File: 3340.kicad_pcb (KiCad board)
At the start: 2 copper layers, 110.5 x 106.7 mm, 181 parts, among them J1 Conn_01x17, J10 FM1, J11 Conn_01x17, J12 V/OCT2, J13 PULSE2, J14 SAW2, J15 TRI2, J16 SINE2, J17 SYNC2, J18 Conn_01x17, J19 PWM2, J2 Conn_01x17, J20 FM2, J3 V/OCT1, J4 PULSE1, J5 SAW1, J6 TRI1, J7 SINE1, J8 SYNC1, J9 PWM1, Q1 2N3904, Q2 2N3906, Q3 2N3904, Q4 2N3906, Q5 2N3904, Q6 2N3904, SW2 DPDT_OOO, U1 TL072, U2 TL074, U3 CEM3340, U4 TL072, U5 CEM3340, U6 TL074

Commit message: Fix electrolytic footprints
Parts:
- removed D7, D8: 1N5818, Diode_THT:D_DO-41_SOD81_P10.16mm_Horizontal
- removed PWR2: PWR, Connector_IDC:IDC-Header_2x05_P2.54mm_Vertical
- moved PWR1 230.2 mm to (19.6, 132.1)
- moved D1 230.2 mm to (27.7, 150.1)
- moved D2 230.2 mm to (27.7, 153.7)
- moved J1 76.4 mm to (121.3, 47.0)
- moved COARSE2 0.65 mm to (41.9, 26.0)
- moved FINE2 0.65 mm to (54.6, 26.0)
- moved J13 0.65 mm to (45.1, 91.4)
- moved J14 0.65 mm to (57.8, 91.4)
- moved J15 0.65 mm to (45.1, 105.3)
- moved J16 0.65 mm to (57.8, 105.3)
- moved J19 0.65 mm to (42.5, 73.6)
- moved J4 0.65 mm to (18.4, 91.4)
- moved J5 0.65 mm to (31.1, 91.4)
- moved J6 0.65 mm to (18.4, 105.3)
- moved J7 0.65 mm to (31.1, 105.3)
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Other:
- board size 110.5 x 106.7 mm -> 110.5 x 106 mm

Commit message: Start backboard 1
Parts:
- C14, C15: footprint Capacitor_THT:C_Disc_D4.3mm_W1.9mm_P5.00mm -> Capacitor_THT:CP_Radial_D5.0mm_P2.00mm
- moved C5 302.4 mm to (86.0, 17.0)
- moved C13 301.6 mm to (64.0, 59.0)
- moved TRK1 287.2 mm to (95.0, 94.0)
- moved C14 287.1 mm to (75.6, 112.3), turned to -90 degrees
- moved R26 278.1 mm to (66.0, 48.0)
- moved U1 277.9 mm to (103.5, 62.9), turned to 180 degrees
- moved C12 276.2 mm to (70.0, 80.0)
- moved R27 273.8 mm to (79.0, 52.0)
- moved C15 265.2 mm to (75.6, 96.8), turned to -90 degrees
- moved R1 264.8 mm to (93.4, 59.7), turned to 180 degrees
- moved R28 261.4 mm to (64.0, 54.0)
- moved C19 260.8 mm to (70.0, 73.0)
- moved D4 258.6 mm to (74.9, 93.3), turned to 180 degrees
- moved R6 256.1 mm to (85.0, 112.0)
- moved C4 254.0 mm to (69.0, 66.0)
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
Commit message: Use autoplace from here
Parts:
- moved C18 270.4 mm to (101.6, 72.7), turned to 180 degrees
- moved R40 269.2 mm to (74.9, 38.7)
- moved C6 168.0 mm to (126.4, 194.3)
- moved C7 161.7 mm to (126.4, 181.6)
- moved D1 158.5 mm to (132.1, 185.4)
- moved C16 144.3 mm to (126.4, 186.1)
- moved C13 139.4 mm to (121.3, 186.1)
- moved R14 135.6 mm to (130.2, 156.8)
- moved R19 125.6 mm to (116.8, 156.8)
- moved R34 124.1 mm to (76.8, 143.9)
- moved C12 121.8 mm to (121.3, 190.5)
- moved R28 118.6 mm to (130.2, 152.4)
- moved R17 118.4 mm to (130.8, 144.8)
- moved C8 118.3 mm to (126.4, 190.5)
- moved R27 107.5 mm to (117.5, 152.4)
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
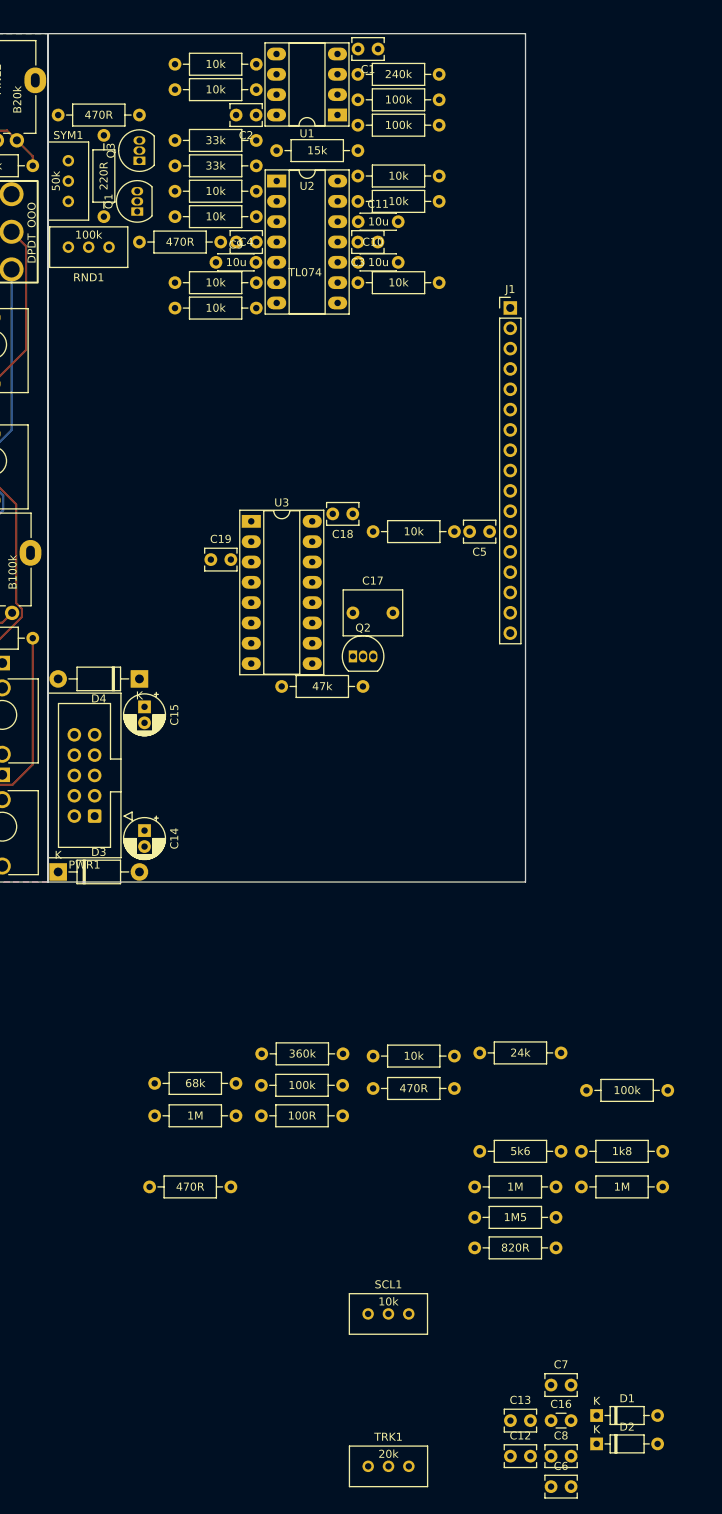
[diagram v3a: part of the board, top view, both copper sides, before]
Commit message: Fix PWM2 connection
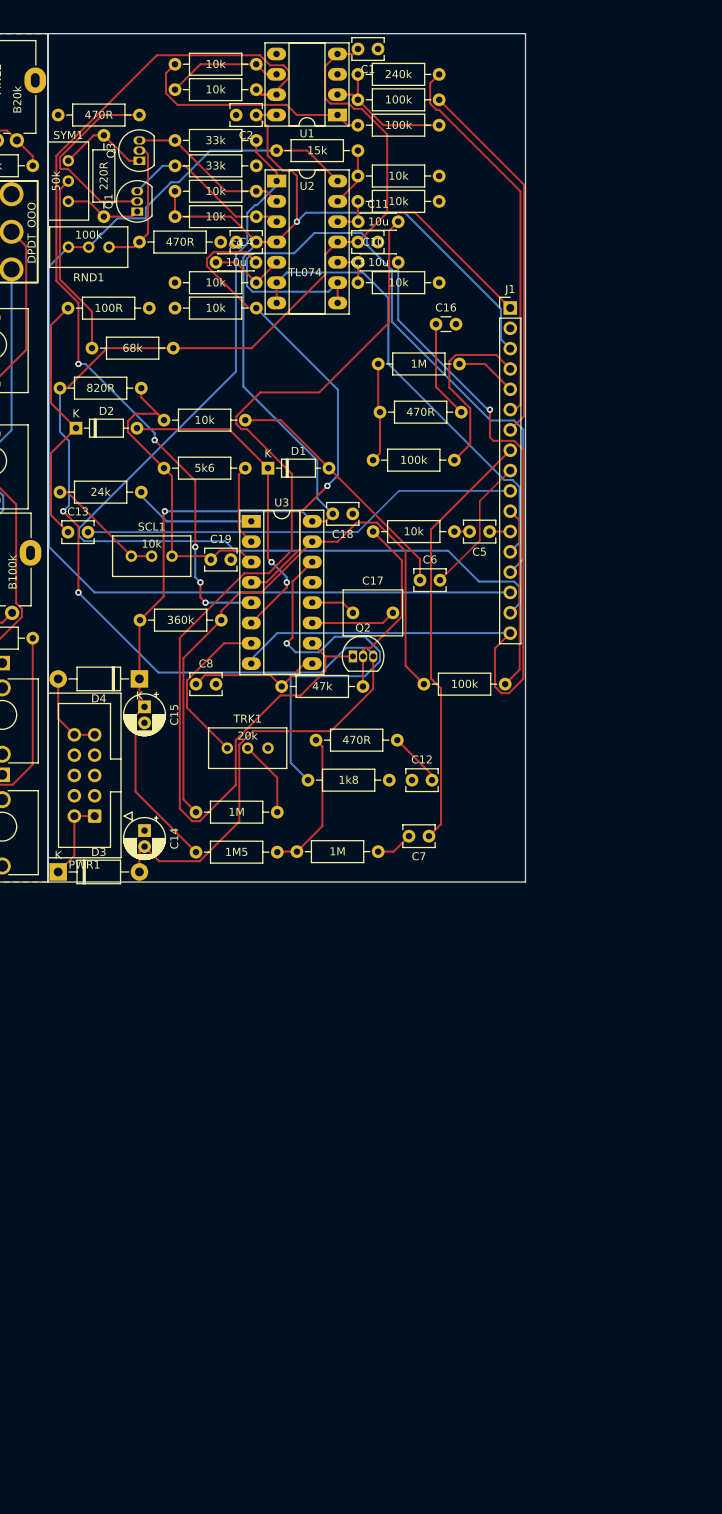
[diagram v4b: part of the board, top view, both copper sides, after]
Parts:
- moved D2 142.7 mm to (67.0, 62.0)
- moved C16 137.8 mm to (112.0, 49.0)
- moved D1 125.3 mm to (91.0, 67.0)
- moved C13 124.1 mm to (66.0, 75.0)
- moved R20 119.3 mm to (65.0, 57.0)
- moved C6 114.5 mm to (110.0, 81.0)
- moved C8 106.2 mm to (82.0, 94.0)
- moved R11 103.8 mm to (66.0, 47.0)
- moved R19 102.9 mm to (114.9, 54.0), turned to 180 degrees
- moved SCL1 99.2 mm to (79.0, 78.0)
- moved R27 94.1 mm to (78.0, 67.0)
- moved R34 92.2 mm to (69.0, 52.0)
- moved TRK1 91.5 mm to (91.0, 102.0)
- moved R26 87.6 mm to (65.0, 70.0)
- moved C12 85.4 mm to (109.0, 106.0)
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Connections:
- U5 pad 5: /PWM1 -> /PWM2
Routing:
- net -12V: track 0.00 -> 221.5 mm, vias 0 -> 2
- net +12V: track 0.00 -> 187.2 mm, vias 0 -> 2
- net /SHAPE1: track 0.00 -> 139.5 mm
- net /TRI1: track 0.00 -> 134.4 mm
- net /SINE1: track 0.00 -> 122.3 mm
- net /PWM1: track 0.00 -> 112.9 mm, vias 0 -> 5
- net /SAW1: track 0.00 -> 106.6 mm, vias 0 -> 1
- net Net-(R17-Pad2): track 0.00 -> 86.9 mm
- net /SAWOUT1: track 0.00 -> 86.9 mm
- net /PULSE1: track 0.00 -> 60.4 mm, vias 0 -> 1
- net /PULSEOUT1: track 0.00 -> 58.0 mm
- net /SYNC-1: track 0.00 -> 54.9 mm
- net /FMOD1: track 0.00 -> 53.5 mm
- net Net-(R28-Pad1): track 0.00 -> 52.2 mm, vias 0 -> 1
- net /PW_IN1: track 0.00 -> 48.1 mm
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
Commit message: Finish backboard 1
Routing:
- net Net-(R14-Pad2): track 18.1 -> 72.0 mm, vias 0 -> 2
- net Net-(R17-Pad2): track 86.9 -> 105.6 mm, vias 0 -> 2
- net -12V: track 221.5 -> 223.4 mm
- net /TRI1: track 134.4 -> 135.6 mm
- net GND: vias 0 -> 3

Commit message: Start backboard 2
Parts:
- removed C37, C38: 10u, Capacitor_THT:C_Disc_D4.3mm_W1.9mm_P5.00mm
- moved C32 253.3 mm to (137.2, 24.8)
- moved Q4 237.8 mm to (159.4, 83.5)
- moved R42 230.8 mm to (143.5, 91.4), turned to 90 degrees
- moved C20 229.1 mm to (158.8, 91.4)
- moved C25 221.6 mm to (137.2, 100.3), turned to -90 degrees
- moved C31 215.1 mm to (143.6, 30.5), turned to 180 degrees
- moved C26 215.0 mm to (173.3, 114.3), turned to 180 degrees
- moved SCL2 212.8 mm to (137.8, 76.8), turned to -90 degrees
- moved C28 212.0 mm to (153.7, 61.6)
- moved R81 208.6 mm to (143.6, 44.5), turned to 180 degrees
- moved C35 200.4 mm to (141.1, 36.2)
- moved Q5 200.1 mm to (171.1, 41.9), turned to -90 degrees
- moved R41 200.0 mm to (163.2, 91.4)
- moved R70 199.4 mm to (166.4, 45.1), turned to 180 degrees
- moved C21 192.8 mm to (137.2, 82.6), turned to -90 degrees
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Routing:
- net Net-(C29-Pad1): track 0.00 -> 44.3 mm
- net /SHAPE2: track 0.00 -> 42.7 mm
- net Net-(R60-Pad2): track 0.00 -> 41.3 mm
- net +12V: track 187.2 -> 222.7 mm
- net Net-(Q6-Pad2): track 0.00 -> 30.5 mm
- net Net-(Q6-Pad3): track 0.00 -> 27.2 mm
- net Net-(D5-Pad1): track 0.00 -> 25.8 mm
- net Net-(Q5-Pad3): track 0.00 -> 22.1 mm
- net Net-(R45-Pad2): track 0.00 -> 17.6 mm
- net Net-(R79-Pad2): track 0.00 -> 14.2 mm
- net Net-(R49-Pad2): track 0.00 -> 14.0 mm
- net /PWM2: track 0.00 -> 13.4 mm
- net Net-(Q6-Pad1): track 0.00 -> 11.5 mm
- net -12V: track 223.4 -> 233.6 mm
- net Net-(Q5-Pad1): track 0.00 -> 9.41 mm
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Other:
- board size 110.5 x 106 mm -> 170.2 x 106.1 mm

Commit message: Finish backboard 2
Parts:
- moved R78 0.68 mm to (170.8, 54.0)
- moved R44 0.66 mm to (137.2, 98.4)
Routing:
- net /SHAPE2: track 42.7 -> 195.5 mm
- net /SINE2: track 3.34 -> 137.3 mm
- net +12V: track 222.7 -> 352.9 mm, vias 2 -> 3
- net /FMOD2: track 0.00 -> 129.7 mm
- net -12V: track 233.6 -> 338.0 mm, vias 2 -> 3
- net /SAW2: track 0.00 -> 85.8 mm
- net /SYNC-2: track 0.00 -> 76.8 mm
- net /SAWOUT2: track 2.54 -> 78.6 mm, vias 0 -> 5
- net /FINE2: track 0.00 -> 68.6 mm
- net /PWM2: track 13.4 -> 80.9 mm
- net /PULSEOUT2: track 2.54 -> 69.7 mm, vias 0 -> 7
- net /V/OCT2: track 0.00 -> 64.3 mm
- net /COARSE2: track 0.00 -> 63.9 mm
- net /PULSE2: track 6.13 -> 56.6 mm
- net /PWM_IN2: track 0.00 -> 50.2 mm
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
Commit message: Fix grid alignment
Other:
- board size 170.2 x 106.1 mm -> 254.7 x 148.1 mm
